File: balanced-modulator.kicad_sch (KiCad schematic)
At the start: 57 parts, among them J1 Conn_02x05_Odd_Even, J10 out, J2 Conn_01x03_Socket, J3 Conn_01x03_Pin, J4 Conn_01x03_Pin, J5 Conn_01x03_Socket, J6 Conn_01x03_Pin, J7 Conn_01x03_Socket, J8 carrier, J9 modulating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

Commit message: board + readme
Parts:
- removed J6: Conn_01x03_Pin, Connector_PinHeader_2.54mm:PinHeader_1x03_P2.54mm_Vertical, symbol Connector:Conn_01x03_Pin
- removed J7: Conn_01x03_Socket, Connector_PinSocket_2.54mm:PinSocket_1x03_P2.54mm_Vertical, symbol Connector:Conn_01x03_Socket
- added H10, H11, H8, H9: MountingHole, MountingHole:MountingHole_2.7mm_M2.5, symbol Mechanical:MountingHole
- C5, C6, C7: footprint Capacitor_THT:C_Rect_L7.2mm_W7.2mm_P5.00mm_FKS2_FKP2_MKS2_MKP2 -> Eurorack:C_Rect_Horizontal_L7.2mm_W11
- JP1, JP2, JP3: footprint Connector_PinHeader_2.54mm:PinHeader_1x03_P2.54mm_Vertical -> Connector_PinHeader_2.54mm:PinHeader_1x03_P2.54mm_Horizontal
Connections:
- net B is gone; now on net B': JP2.1 (A)
- net B_dc is gone; now on net B_dc': JP2.3 (B)
- net A': now also JP1.1 (A); no longer J4.2 (Pin_2)
- net A_dc': now also JP1.3 (B); no longer J4.3 (Pin_3)
- net OUT': now also JP3.1 (A); no longer J3.2 (Pin_2)
- net OUT_dc': now also JP3.3 (B); no longer J3.3 (Pin_3)
- net _B: now reaches R10.1
- net _B: now also J5.3 (Pin_3); no longer JP2.2 (C)
- net _OUT: now reaches R24.2
- net _OUT: now also J2.2 (Pin_2); no longer JP3.2 (C)
- net _A: now reaches R3.1
- net _A: now also J5.2 (Pin_2); no longer JP1.2 (C)
- removed net A: J5.2 (Pin_2), JP1.1 (A)
- removed net A_dc: J5.3 (Pin_3), JP1.3 (B)
- removed net OUT: J2.2 (Pin_2), JP3.1 (A)
- net OUT_dc: no longer names the net of J2.3 (Pin_3)
- net OUT_dc: no longer JP3.3 (B)
- new net _A': J4.2 (Pin_2), JP1.2 (C)
- new net _B': J4.3 (Pin_3), JP2.2 (C)
- new net _OUT': J3.2 (Pin_2), JP3.2 (C)
- no-connect marks 3 -> 5
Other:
- moved on the sheet: JP1, JP2, JP3

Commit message: adding part number
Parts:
- U2: PartNum (none) -> 595-TL072CDR; Vendor (none) -> Mouser
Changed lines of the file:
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@@
+      (effects (font (size 1.27 1.27)) hide)
+    )
+    (property "Vendor" "Mouser" (at 245.11 67.31 0)
+      (effects (font (size 1.27 1.27)) hide)
+    )
+    (property "PartNum" "595-TL072CDR" (at 245.11 67.31 0)
       (effects (font (size 1.27 1.27)) hide)
     )
@@
     )
     (property "Datasheet" "http://www.ti.com/lit/ds/symlink/tl071.pdf" (at 208.28 64.77 0)
+      (effects (font (size 1.27 1.27)) hide)
+    )
+    (property "Vendor" "Mouser" (at 208.28 64.77 0)
+      (effects (font (size 1.27 1.27)) hide)
+    )
+    (property "PartNum" "595-TL072CDR" (at 208.28 64.77 0)
       (effects (font (size 1.27 1.27)) hide)
     )
@@
       (effects (font (size 1.27 1.27)) hide)
     )
+    (property "Vendor" "Mouser" (at 273.05 153.67 0)
+      (effects (font (size 1.27 1.27)) hide)
+    )
+    (property "PartNum" "595-TL072CDR" (at 273.05 153.67 0)
+      (effects (font (size 1.27 1.27)) hide)
+    )

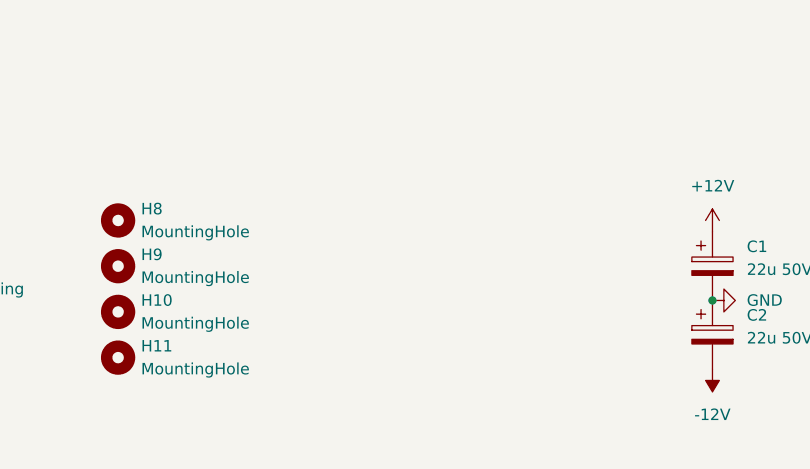
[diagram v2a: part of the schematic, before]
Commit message: ready for v0 manu
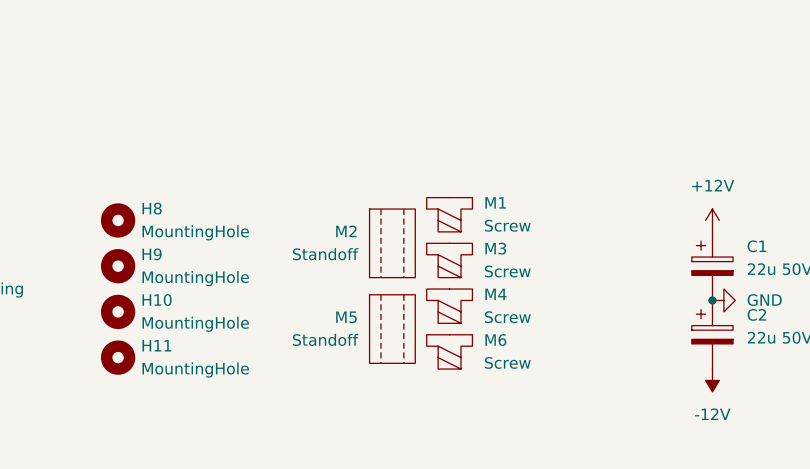
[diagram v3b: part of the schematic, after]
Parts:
- added M1, M3, M4, M6: Screw, Eurorack:Screw_M2.5x0.45-6mm, symbol Eurorack:Screw
- added M2, M5: Standoff, Eurorack:Standoff_M2.5x0.45-11mm, symbol Eurorack:Standoff
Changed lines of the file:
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@@
+    )
+  )
+  (symbol (lib_id "Eurorack:Screw") (at 92.71 179.07 0) (unit 1)
+    (in_bom yes) (on_board yes) (dnp no) (fields_autoplaced)
+    (property "Reference" "M4" (at 96.52 178.435 0)
+      (effects (font (size 1.27 1.27)) (justify left))
+    )
+    (property "Value" "Screw" (at 96.52 180.975 0)
+      (effects (font (size 1.27 1.27)) (justify left))
+    )
+    (property "Footprint" "Eurorack:Screw_M2.5x0.45-6mm" (at 92.71 179.07 0)
+      (effects (font (size 1.27 1.27)) hide)
+    )
+    (property "Datasheet" "" (at 92.71 179.07 0)
+      (effects (font (size 1.27 1.27)) hide)
+    )
+    (property "Vendor" "Digikey" (at 92.71 179.07 0)
+      (effects (font (size 1.27 1.27)) hide)
+    )
+    (property "PartNum" "36-29301-ND" (at 92.71 179.07 0)
+      (effects (font (size 1.27 1.27)) hide)
+    )
+    (instances
+      (project "balanced-modulator"
+        (path "/54607e40-577c-4def-b17c-96859aef0795"
+          (reference "M4") (unit 1)
+        )
+      )
     )
   )
@@
     )
   )
+  (symbol (lib_id "Eurorack:Screw") (at 92.71 184.15 0) (unit 1)
+    (in_bom yes) (on_board yes) (dnp no)
+    (property "Reference" "M6" (at 96.52 183.515 0)
+      (effects (font (size 1.27 1.27)) (justify left))
+    )
+    (property "Value" "Screw" (at 96.52 186.055 0)
+      (effects (font (size 1.27 1.27)) (justify left))
+    )
+    (property "Footprint" "Eurorack:Screw_M2.5x0.45-6mm" (at 92.71 184.15 0)
+      (effects (font (size 1.27 1.27)) hide)
+    )
+    (property "Datasheet" "" (at 92.71 184.15 0)
+      (effects (font (size 1.27 1.27)) hide)
+    )
+    (property "Vendor" "Digikey" (at 92.71 184.15 0)
+      (effects (font (size 1.27 1.27)) hide)
+    )
+    (property "PartNum" "36-29301-ND" (at 92.71 184.15 0)
+      (effects (font (size 1.27 1.27)) hide)
+    )
+    (instances
+      (project "balanced-modulator"
+        (path "/54607e40-577c-4def-b17c-96859aef0795"
+          (reference "M6") (unit 1)
+        )
+      )
+    )
+  )
   (symbol (lib_id "Mechanical:MountingHole") (at 55.88 185.42 0) (unit 1)
     (in_bom no) (on_board yes) (dnp no) (fields_autoplaced)
@@
     )
   )
+  (symbol (lib_id "Eurorack:Standoff") (at 86.36 172.72 0) (unit 1)
+    (in_bom yes) (on_board no) (dnp no)
+    (property "Reference" "M2" (at 82.55 171.45 0)
+      (effects (font (size 1.27 1.27)) (justify right))
+    )
+    (property "Value" "Standoff" (at 82.55 173.99 0)
+      (effects (font (size 1.27 1.27)) (justify right))
+    )
+    (property "Footprint" "Eurorack:Standoff_M2.5x0.45-11mm" (at 86.36 172.72 0)
+      (effects (font (size 1.27 1.27)) hide)
+    )
+    (property "Datasheet" "" (at 86.36 172.72 0)
+      (effects (font (size 1.27 1.27)) hide)
+    )
+    (property "Vendor" "Digikey" (at 86.36 172.72 0)
+      (effects (font (size 1.27 1.27)) hide)
+    )
+    (property "PartNum" "732-10549-ND" (at 86.36 172.72 0)
+      (effects (font (size 1.27 1.27)) hide)
+    )
+    (instances
+      (project "balanced-modulator"
+        (path "/54607e40-577c-4def-b17c-96859aef0795"
+          (reference "M2") (unit 1)
+        )
+      )
+    )
+  )
   (symbol (lib_id "Mechanical:MountingHole_Pad") (at 16.51 193.04 0) (unit 1)
     (in_bom no) (on_board yes) (dnp no) (fields_autoplaced)
@@
         (path "/54607e40-577c-4def-b17c-96859aef0795"
           (reference "C2") (unit 1)
+        )
+      )
+    )
+  )
+  (symbol (lib_id "Eurorack:Standoff") (at 86.36 182.245 0) (unit 1)
+    (in_bom yes) (on_board no) (dnp no)
+    (property "Reference" "M5" (at 82.55 180.975 0)
+      (effects (font (size 1.27 1.27)) (justify right))
+    )
+    (property "Value" "Standoff" (at 82.55 183.515 0)
+      (effects (font (size 1.27 1.27)) (justify right))
+    )
+    (property "Footprint" "Eurorack:Standoff_M2.5x0.45-11mm" (at 86.36 182.245 0)
+      (effects (font (size 1.27 1.27)) hide)
+    )
+    (property "Datasheet" "" (at 86.36 182.245 0)
+      (effects (font (size 1.27 1.27)) hide)
+    )
+    (property "Vendor" "Digikey" (at 86.36 182.245 0)
+      (effects (font (size 1.27 1.27)) hide)
+    )
+    (property "PartNum" "732-10549-ND" (at 86.36 182.245 0)
+      (effects (font (size 1.27 1.27)) hide)
+    )
+    (instances
+      (project "balanced-modulator"
+        (path "/54607e40-577c-4def-b17c-96859aef0795"
+          (reference "M5") (unit 1)
         )
       )
@@
     )
   )
+  (symbol (lib_id "Eurorack:Screw") (at 92.71 168.91 0) (unit 1)
+    (in_bom yes) (on_board yes) (dnp no) (fields_autoplaced)
+    (property "Reference" "M1" (at 96.52 168.275 0)
+      (effects (font (size 1.27 1.27)) (justify left))
+    )
+    (property "Value" "Screw" (at 96.52 170.815 0)
+      (effects (font (size 1.27 1.27)) (justify left))
+    )
+    (property "Footprint" "Eurorack:Screw_M2.5x0.45-6mm" (at 92.71 168.91 0)
+      (effects (font (size 1.27 1.27)) hide)
+    )
+    (property "Datasheet" "" (at 92.71 168.91 0)
+      (effects (font (size 1.27 1.27)) hide)
+    )
+    (property "Vendor" "Digikey" (at 92.71 168.91 0)
+      (effects (font (size 1.27 1.27)) hide)
+    )
+    (property "PartNum" "36-29301-ND" (at 92.71 168.91 0)
+      (effects (font (size 1.27 1.27)) hide)
+    )
+    (instances
+      (project "balanced-modulator"
+        (path "/54607e40-577c-4def-b17c-96859aef0795"
+          (reference "M1") (unit 1)
+        )
+      )
+    )
+  )
   (symbol (lib_id "Device:R") (at 119.38 82.55 180) (unit 1)
     (in_bom yes) (on_board yes) (dnp no)
@@
         )
       )
+    )
+  )
+  (symbol (lib_id "Eurorack:Screw") (at 92.71 173.99 0) (unit 1)
+    (in_bom yes) (on_board yes) (dnp no)
+    (property "Reference" "M3" (at 96.52 173.355 0)
+      (effects (font (size 1.27 1.27)) (justify left))
+    )
+    (property "Value" "Screw" (at 96.52 175.895 0)
+      (effects (font (size 1.27 1.27)) (justify left))
+    )
+    (property "Footprint" "Eurorack:Screw_M2.5x0.45-6mm" (at 92.71 173.99 0)
+      (effects (font (size 1.27 1.27)) hide)
+    )
+    (property "Datasheet" "" (at 92.71 173.99 0)
+      (effects (font (size 1.27 1.27)) hide)
+    )
+    (property "Vendor" "Digikey" (at 92.71 173.99 0)
+      (effects (font (size 1.27 1.27)) hide)
+    )
+    (property "PartNum" "36-29301-ND" (at 92.71 173.99 0)
+      (effects (font (size 1.27 1.27)) hide)
+    )
+    (instances
+      (project "balanced-modulator"
+        (path "/54607e40-577c-4def-b17c-96859aef0795"
+          (reference "M3") (unit 1)
+        )
+      )
